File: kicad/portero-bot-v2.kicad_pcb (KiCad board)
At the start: 2 copper layers, 81 parts, among them J1 DC005, J2 HR911105A, J3 USB Micro B, J7 Pin Header 01x04 2.54mm Verti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, K1 SRD-05VDC-SL-C, K2 SRD-05VDC-SL-C, K3 SRD-05VDC-SL-C, Q1 2N2222A, Q2 2N2222A, Q3 2N2222A, U1 ESP32-WROOM-32E-N16, U2 W5500, U3 CH340C, U4 MP2307DN-HW-LF-Z, U5 MP2307DN-HW-LF-Z, Y1 NX3225GA-25MHZ-STD-CRG-2

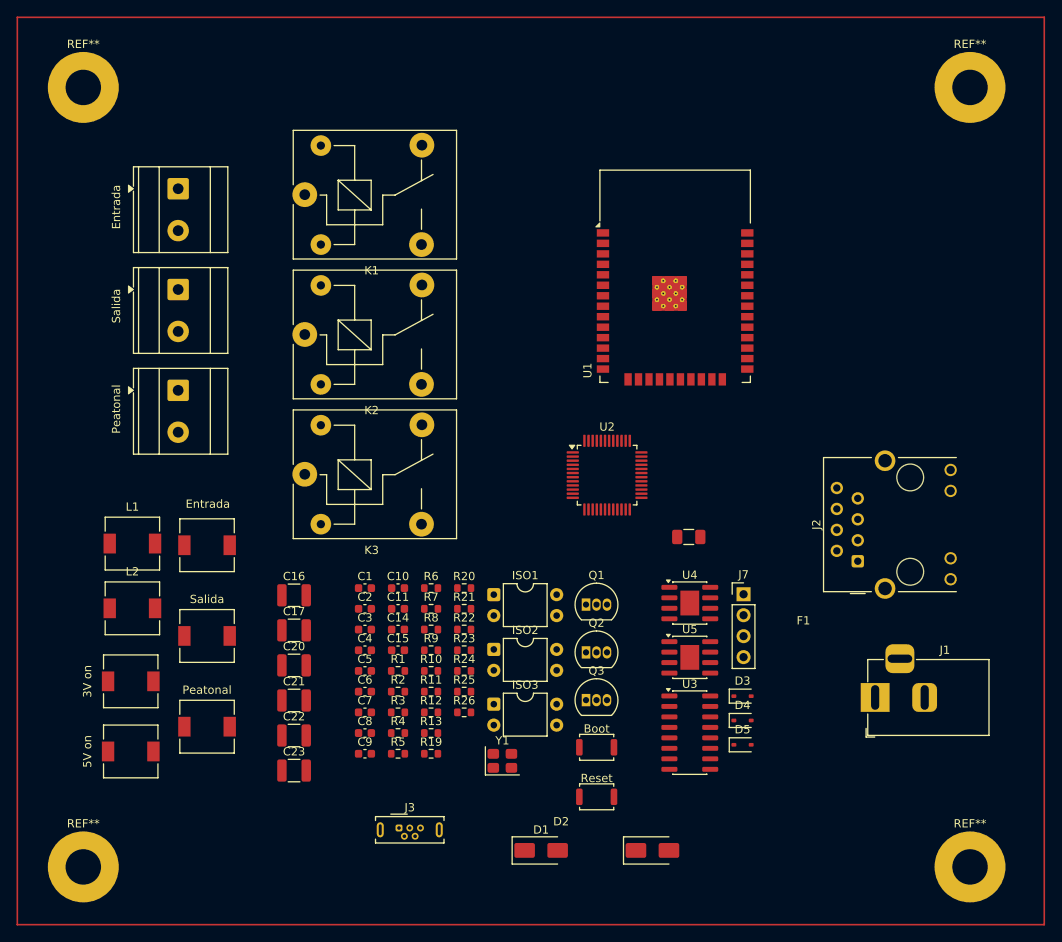
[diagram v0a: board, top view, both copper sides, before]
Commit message: feat(pcb): rute RELAY1_GPIO/BOOT/BST_5V con A* multilayer, 0 unconnected
3 redes ruteadas programáticamente con A* sobre grid 0.5mm en F.Cu+B.Cu:
- RELAY1_GPIO (R7.1 ↔ U1.8): 4 vías, 23 segmentos
- BOOT (R2.2 ↔ SW1.1 ↔ U1.25): 4 vías, 59 segmentos
- BST_5V (C22.1 ↔ U4.1): 6 vías, 23 segmentos

Verificador con line-segment intersection + circle distance evita shorts,
respeta keep-out antena ESP32 (x=122.25-170.25, y=47.145-68.085).

Eliminados componentes (script 59) según pedido del cliente:
- LED2, LED3, LED4 (indicadores de relé)
- R10, R11, R12 (resistencias series de los LEDs)

DRC: 300 → 100 violations (0 unconnected, 0 shorts, 0 keep-out hits,
0 tracks_crossing). Restantes son clearances pre-existentes del freerouting
todos <0.10mm. Regla clearance_jlcpcb relajada a 0.10mm.

Scripts del pipeline:
- 56a_clean: limpia nets target + bad zero-drill vias
- 58a_explore: extrae endpoints, vías cercanas, keep-out zones
- 58b_probe_corridors: mapea corredores B.Cu claros (horizontales + verticales)
- 58c_astar: A* monolayer (precursor, no usado finalmente)
- 58d_multilayer: A* multilayer F.Cu+B.Cu con vías intermedias (router final)
- 59_remove_relay_leds: elimina LEDs + resistencias de indicadores de relé

Co-Authored-By: Claude Opus 4.7 <noreply@anthropic.com>
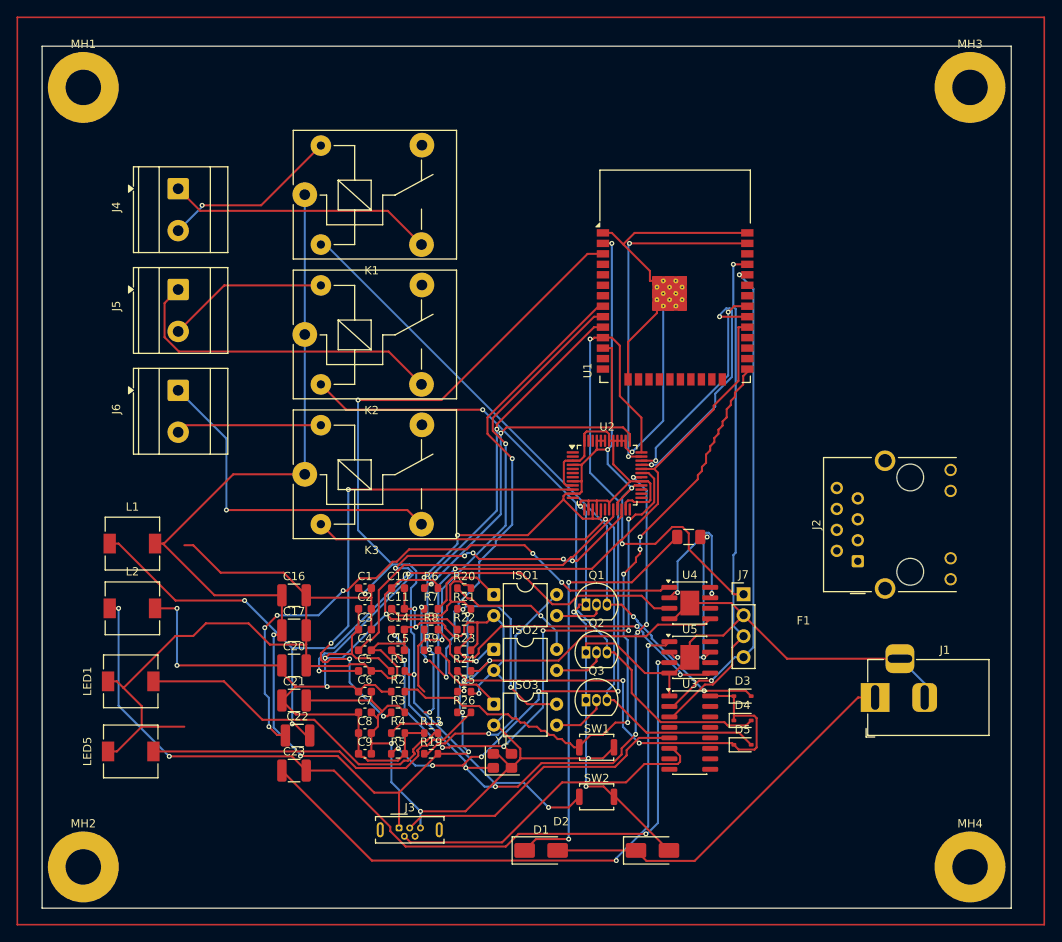
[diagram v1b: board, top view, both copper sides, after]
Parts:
- removed Entrada, Peatonal, Salida: KT-0603R, Inductor_SMD:L_6.3x6.3_H3
- removed R10, R11, R12: 1k, Resistor_SMD:R_0603_1608Metric
- LED1: renamed from 3V on
- LED5: renamed from 5V on
- moved C22 0.42 mm to (100.5, 130.6)
- renumbered Entrada to J4, Salida to J5, Peatonal to J6, REF** to MH1, REF** to MH2, REF** to MH3, REF** to MH4, Boot to SW1, Reset to SW2
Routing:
- net GND: track 0.00 -> 454.1 mm, vias 0 -> 10
- net 3V3: track 0.00 -> 222.0 mm, vias 0 -> 11
- net 5V: track 0.00 -> 214.1 mm, vias 0 -> 8
- net EN: track 0.00 -> 111.4 mm, vias 0 -> 4
- net SW_BUCK_3V3: track 0.00 -> 107.7 mm, vias 0 -> 4
- net ETH_INT: track 0.00 -> 95.2 mm, vias 0 -> 6
- net SW_BUCK: track 0.00 -> 91.0 mm, vias 0 -> 3
- net ETH_CS: track 0.00 -> 82.5 mm, vias 0 -> 2
- net ETH_XI: track 0.00 -> 81.9 mm, vias 0 -> 7
- net RELAY1_COIL_LOW: track 0.00 -> 80.7 mm, vias 0 -> 2
- net BOOT: track 0.00 -> 80.6 mm, vias 0 -> 4
- net RELAY2_COIL_LOW: track 0.00 -> 79.6 mm, vias 0 -> 1
- net RELAY3_COIL_LOW: track 0.00 -> 78.7 mm, vias 0 -> 1
- net BST_3V3: track 0.00 -> 75.5 mm, vias 0 -> 2
- net ETH_XO: track 0.00 -> 72.0 mm, vias 0 -> 6
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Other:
- board outline added: 117.5 x 104.5 mm

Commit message: feat(pcb): re-ruteo completo con freerouting v2.2.4, DRC 100% limpio
- Netclass Default: añade via_diameter 0.6mm + via_drill 0.3mm + clearance 0.10mm
  (fix bug que generaba 79 shorts: KiCad exportaba vias -0.001mm sin estas dims)
- Re-routing freerouting v2.2.4 (Java 25): 191 nets, 0 unrouted en pass #10
- DRC: 0 violations, 0 unconnected, 0 footprint errors
- 928 trazas/vías totales
- scripts/60_clean_and_export_dsn.py: wipe tracks/vias + ExportSpecctraDSN
- scripts/61_import_ses.py: ImportSpecctraSES

Co-Authored-By: Claude Opus 4.7 <noreply@anthropic.com>
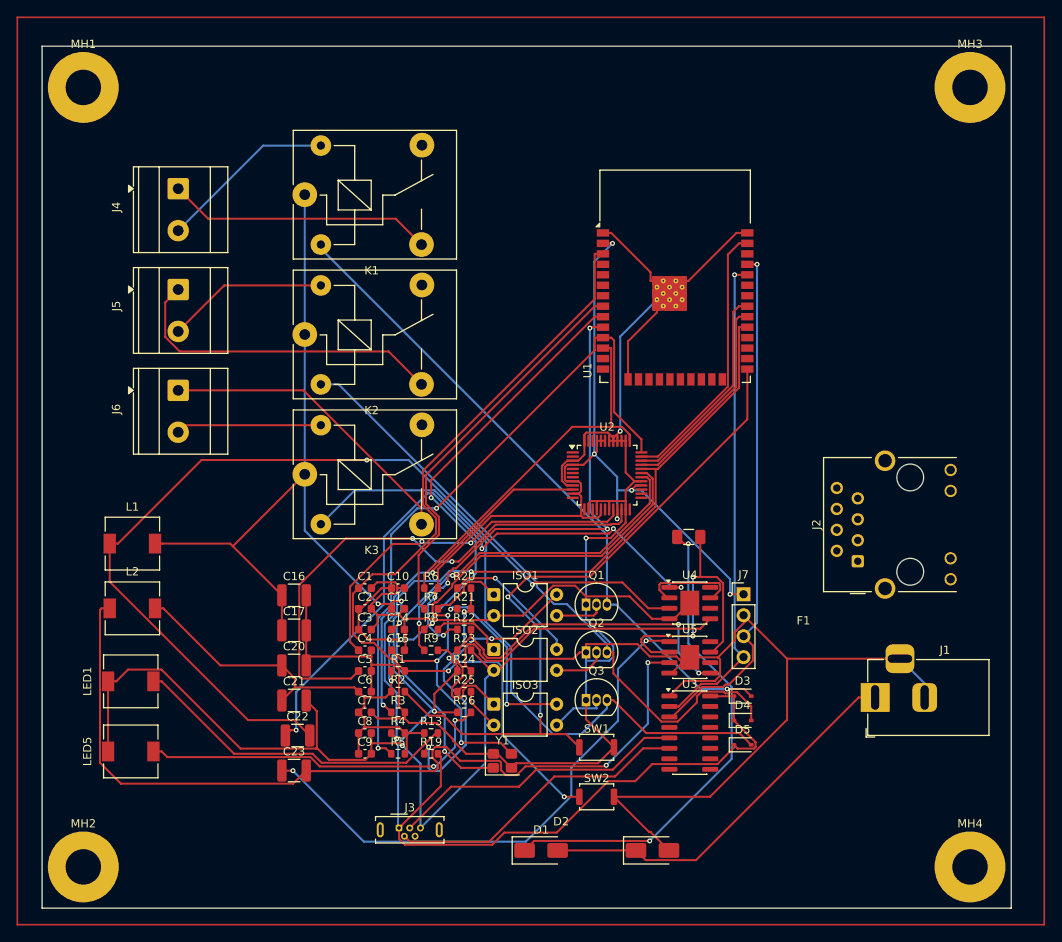
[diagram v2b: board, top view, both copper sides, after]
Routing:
- net GND: track 454.1 -> 486.3 mm, vias 10 -> 3
- net 3V3: track 222.0 -> 191.4 mm, vias 11 -> 10
- net SW_BUCK: track 91.0 -> 116.4 mm, vias 3 -> 2
- net W5500_EXRES: track 62.7 -> 42.3 mm, vias 4 -> 2
- net RELAY1_GPIO: track 66.2 -> 48.1 mm, vias 4 -> 0
- net ETH_XI: track 81.9 -> 66.5 mm, vias 7 -> 3
- net Net 2: track 21.1 -> 35.8 mm, vias 3 -> 2
- net ETH_INT: track 95.2 -> 81.3 mm, vias 6 -> 2
- net BST_3V3: track 75.5 -> 66.4 mm
- net SPI_MOSI: track 41.8 -> 32.9 mm, vias 2 -> 0
- net W5500_1V2O: track 56.0 -> 64.8 mm, vias 6 -> 2
- net EN: track 111.4 -> 103.5 mm, vias 4 -> 2
- net RELAY2_GPIO: track 59.5 -> 52.1 mm
- net RELAY1_OPTO_COL: track 29.9 -> 37.2 mm, vias 1 -> 2
- net VIN_PROT: track 52.5 -> 59.6 mm
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
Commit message: fix(pcb): J2 RJ45 net assignment + filter LEDs/Rs de relé
Bug crítico: J2 (HR911105A) tenía los 8 pads con net='' por pines
anónimos en EDIF de Flux. DRC reportaba "0 unconnected" porque solo
cuenta pads-con-red-sin-traza — placa quedó sin Ethernet conectado y
"limpia" hasta inspección visual del 3D.

Pad map confirmado vs Connector.kicad_sym:
  1=TD+/ETH_TX_P  2=TD-/ETH_TX_N  3=RD+/ETH_RX_P
  4=TCT/3V3       5=RCT/3V3       6=RD-/ETH_RX_N
  SH×2=GND        7-12=NC

Cambios:
- scripts/26_fix_j2_pinmap.py: renombra J2.~ → pin numbers en nets_clean
- scripts/62_assign_j2_nets_pcb.py: SetNet directo en .kicad_pcb (idempotente)
- scripts/30_gen_schematic.py: padmap J2 + no sobreescribir .kicad_pro existente
- scripts/25_remove_relay_leds_from_master.py: filtra LED2/3/4 + R10/11/12
- scripts/10_parse_edif.py: pipeline parse EDIF → nets_clean.json

Estado post-re-routing #3 (freerouting v2.2.4):
  199 nets → 1 unrouted (U5.2↔U5.7 MP2307 EN-IN tie, schematic original)
  DRC: 0 violations + 1 unconnected residual

.gitignore: excluir DRC reports, backups .bak-*, .dsn/.ses, kicad_prl,
lockfiles y .history/ — ruido transitorio del flujo.

Co-Authored-By: Claude Opus 4.7 <noreply@anthropic.com>
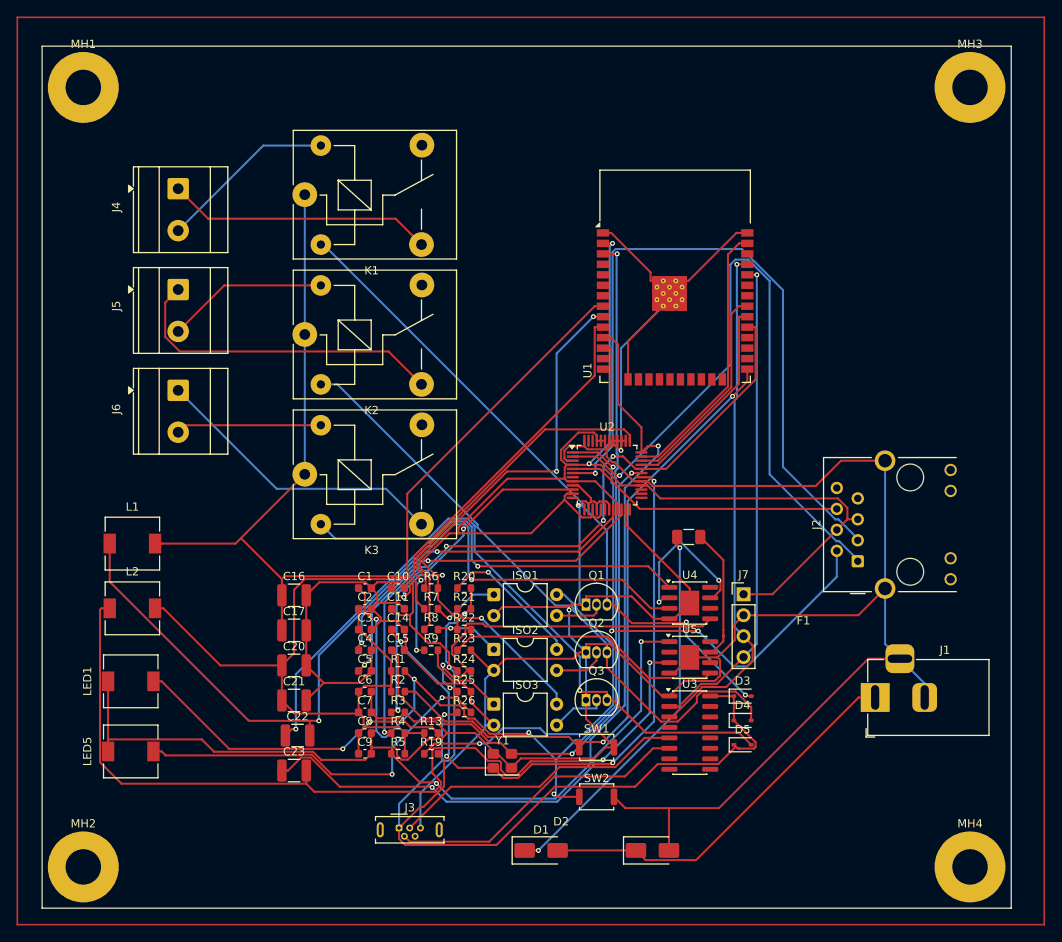
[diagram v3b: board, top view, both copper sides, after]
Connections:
- J2 pad 1: (no net) -> ETH_TX_P
- J2 pad 2: (no net) -> ETH_TX_N
- J2 pad 3: (no net) -> ETH_RX_P
- J2 pad 4: (no net) -> 3V3
- J2 pad 5: (no net) -> 3V3
- J2 pad 6: (no net) -> ETH_RX_N
- J2 pad SH: (no net) -> GND
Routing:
- net ETH_RX_P: track 0.00 -> 87.6 mm, vias 0 -> 1
- net ETH_TX_P: track 0.00 -> 82.5 mm, vias 0 -> 1
- net 3V3: track 191.4 -> 260.9 mm, vias 10 -> 4
- net ETH_TX_N: track 0.00 -> 62.5 mm, vias 0 -> 3
- net GND: track 486.3 -> 538.2 mm
- net ETH_RX_N: track 0.00 -> 34.0 mm
- net EN: track 103.5 -> 125.9 mm, vias 2 -> 5
- net W5500_1V2O: track 64.8 -> 43.7 mm
- net Net 2: track 35.8 -> 15.9 mm, vias 2 -> 0
- net SW_BUCK: track 116.4 -> 103.4 mm
- net VIN_PROT: track 59.6 -> 46.9 mm
- net ETH_XI: track 66.5 -> 78.3 mm, vias 3 -> 4
- net RELAY3_COIL_LOW: track 79.6 -> 70.1 mm, vias 0 -> 1
- net BST_5V: track 76.3 -> 66.9 mm, vias 4 -> 2
- net RELAY3_GPIO: track 59.8 -> 50.8 mm, vias 4 -> 2
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
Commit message: feat(pcb): 3D models + silkscreen labels + manual EN-IN ties
3D models faltantes en stock KiCad 10 substituidos por equivalentes
visuales del mismo paquete (footprints intactos):
  J2 (RJ45): Hanrun HR911105A -> Pulse JK0654219NL
  J3 (USB):  Wuerth 614105150721 -> Molex 47346-0001
  L1/L2:     L_6.3x6.3_H3 -> L_TechFuse_SL0630

Silkscreen labels agregados en F.Silkscreen:
  ENTRADA  (sobre J4/K1)
  SALIDA   (sobre J5/K2)
  PEATONAL (sobre J6/K3)
  RESET    (junto a SW1)
  BOOT     (junto a SW2)

Re-routing 4 con freerouting v2.2.4 tras componentes movidos por user:
  199 nets -> 1 unrouted (VIN_BUCK U4.7<->U4.2, MP2307 EN-IN tie)

Trazas manuales agregadas para cerrar EN-IN ties:
  U4.2 <-> U4.7 (5V buck), 2 vias 0.6mm + segmento B.Cu
  U5.2 <-> U5.7 (3.3V buck), F.Cu rodeando body

51_fix_via_sizes.py corrigio 2 vias 0mm (bug netclass) a 0.6/0.3mm.

Scripts nuevos:
  63_substitute_3d_models.py: substitucion paths .step
  64_add_silkscreen_labels.py: agrega gr_text F.Silkscreen
  65_fix_via_clearance.py: utility para mover via + endpoints (no usado finalmente)

Estado: DRC 0 errors, 0 unconnected, 0 footprint errors. JLCPCB-ready.

Co-Authored-By: Claude Opus 4.7 <noreply@anthropic.com>
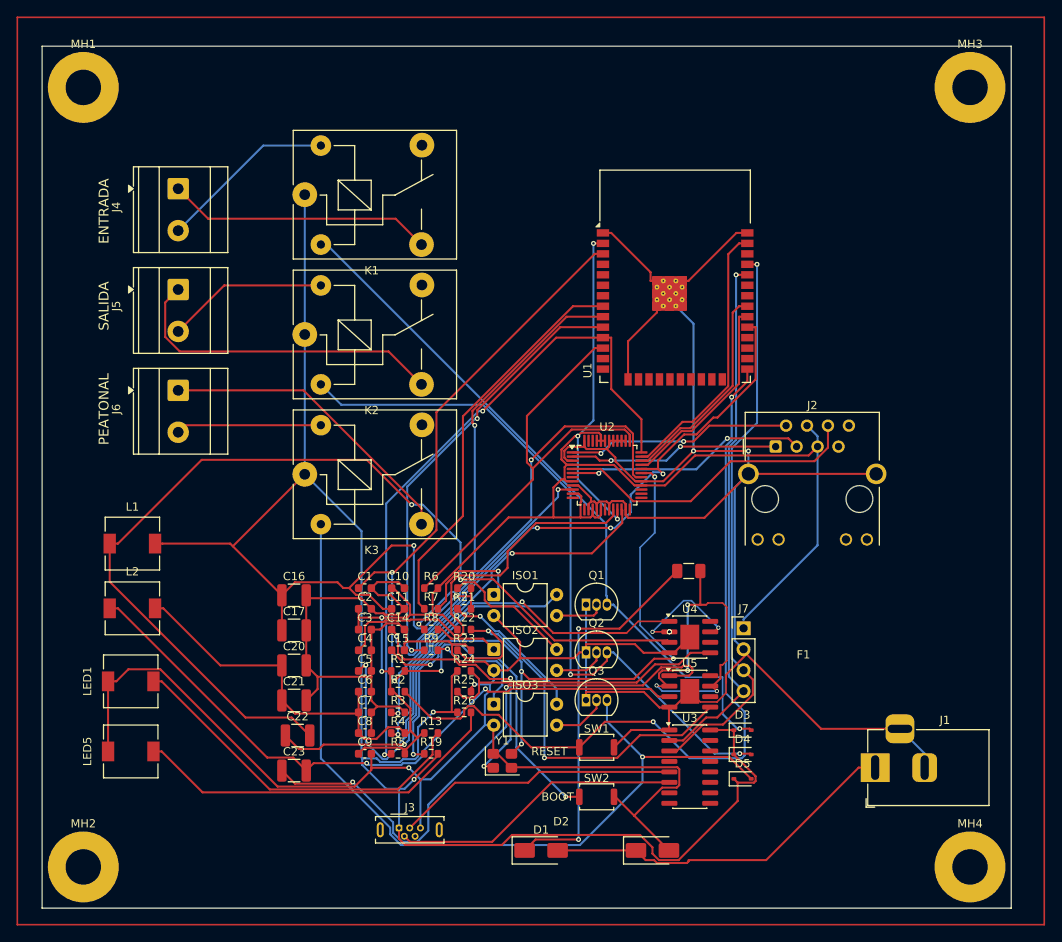
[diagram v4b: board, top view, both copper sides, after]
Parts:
- moved J2 17.1 mm to (158.4, 95.5), turned to 0 degrees
- moved J1 8.50 mm to (170.5, 134.5)
- moved D4 4.12 mm to (154.4, 132.9)
- moved D5 4.12 mm to (154.4, 135.8)
- moved F1 4.12 mm to (147.9, 110.6)
- moved J7 4.12 mm to (154.5, 117.6)
- moved U3 4.12 mm to (148.0, 134.3)
- moved U4 4.12 mm to (148.0, 118.6)
- moved U5 4.12 mm to (148.0, 125.2)
- moved D3 4.12 mm to (154.4, 129.9)
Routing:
- net ETH_RX_P: track 87.6 -> 29.3 mm, vias 1 -> 2
- net ETH_TX_P: track 82.5 -> 25.5 mm, vias 1 -> 2
- net GND: track 538.2 -> 493.4 mm, vias 3 -> 4
- net 5V: track 216.1 -> 254.4 mm, vias 3 -> 4
- net ETH_TX_N: track 62.5 -> 27.3 mm, vias 3 -> 2
- net RELAY3_COIL_LOW: track 70.1 -> 101.4 mm
- net Net 2: track 15.9 -> 43.9 mm, vias 0 -> 4
- net SW_BUCK_3V3: track 109.1 -> 81.2 mm
- net EN: track 125.9 -> 106.6 mm, vias 5 -> 4
- net FB_3V3: track 34.5 -> 53.3 mm, vias 0 -> 2
- net 3V3: track 260.9 -> 242.7 mm, vias 4 -> 5
- net W5500_1V2O: track 43.7 -> 61.9 mm
- net BOOT: track 79.6 -> 97.7 mm
- net SW_BUCK: track 103.4 -> 120.5 mm
- net RELAY2_COIL_LOW: track 75.5 -> 86.5 mm, vias 0 -> 2
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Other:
- board text added: "BOOT"
- board text added: "ENTRADA"
- board text added: "PEATONAL"
- board text added: "RESET"
- board text added: "SALIDA"
